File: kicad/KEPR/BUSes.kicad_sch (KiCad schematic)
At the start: 0 parts

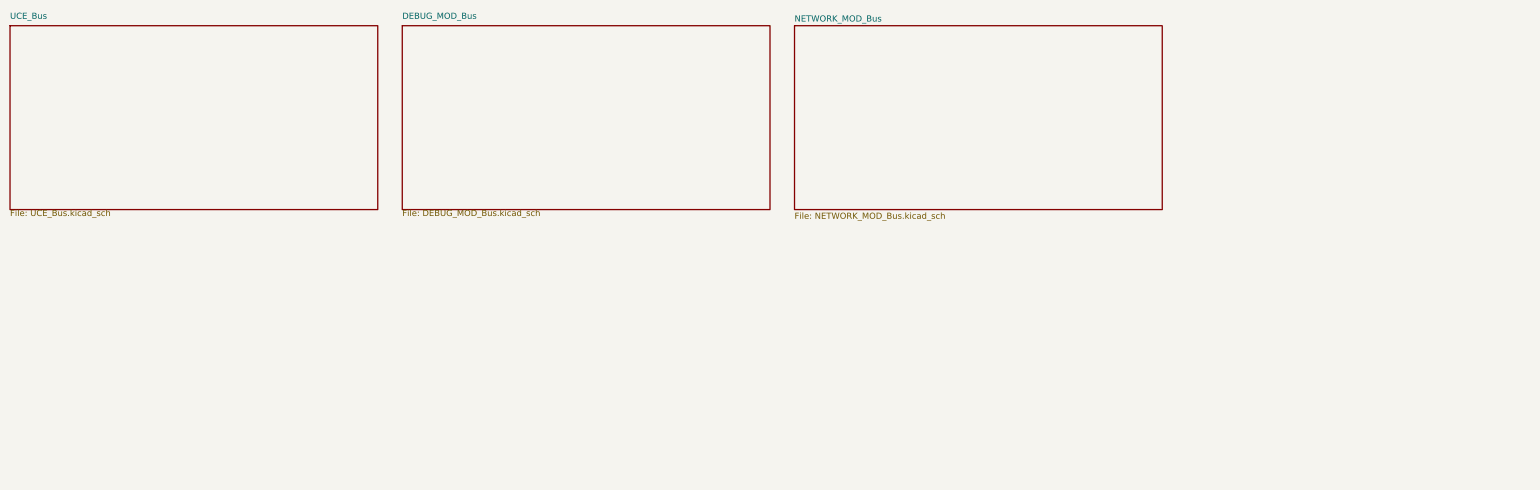
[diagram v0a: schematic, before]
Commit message: Definido os demais buses, criado folha do carimbo, versão 0.5
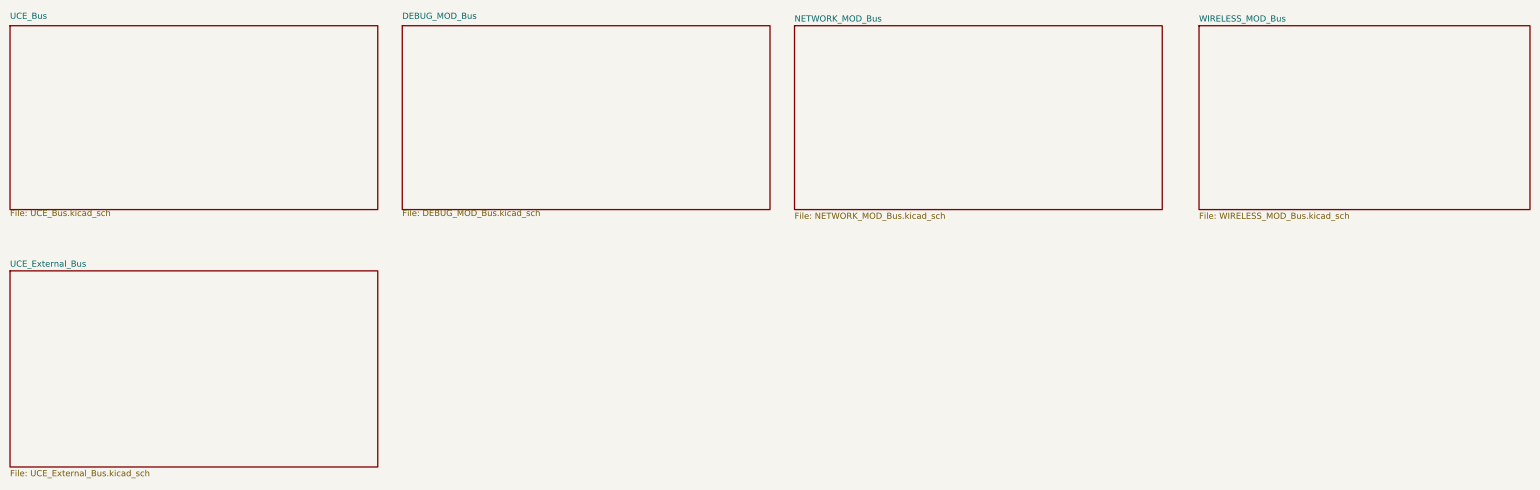
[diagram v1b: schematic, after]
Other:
- added sheet UCE_External_Bus (UCE_External_Bus.kicad_sch)
- added sheet WIRELESS_MOD_Bus (WIRELESS_MOD_Bus.kicad_sch)
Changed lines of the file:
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@@
 		)
 		(fill
-			(color 0 0 0 0.0000)
+			(color 255 73 85 1.0000)
 		)
 		(property "Sheetname" "DEBUG_MOD_Bus"
@@
 			(project "KEPR"
 				(path "/5d9e1dfb-5ec5-4e06-bbdb-9cbfa1c0b9f1/0260e008-78ae-4c2c-85f8-b31739d2ea08"
-					(page "1")
+					(page "A00103")
+				)
+			)
+		)
+	)
+	(sheet
+		(at 33.02 76.2)
+		(size 76.2 40.64)
+		(exclude_from_sim no)
+		(in_bom yes)
+		(on_board yes)
+		(dnp no)
+		(fields_autoplaced yes)
+		(stroke
+			(width 0.1524)
+			(type solid)
+		)
+		(fill
+			(color 255 75 79 1.0000)
+		)
+		(property "Sheetname" "UCE_External_Bus"
+			(at 33.02 75.4884 0)
+			(effects
+				(font
+					(size 1.27 1.27)
+				)
+				(justify left bottom)
+			)
+		)
+		(property "Sheetfile" "UCE_External_Bus.kicad_sch"
+			(at 33.02 117.4246 0)
+			(effects
+				(font
+					(size 1.27 1.27)
+				)
+				(justify left top)
+			)
+		)
+		(instances
+			(project "KEPR"
+				(path "/5d9e1dfb-5ec5-4e06-bbdb-9cbfa1c0b9f1/0260e008-78ae-4c2c-85f8-b31739d2ea08"
+					(page "A00105")
 				)
 			)
@@
 		)
 		(fill
-			(color 0 0 0 0.0000)
+			(color 255 73 85 1.0000)
 		)
 		(property "Sheetname" "NETWORK_MOD_Bus"
@@
 			(project "KEPR"
 				(path "/5d9e1dfb-5ec5-4e06-bbdb-9cbfa1c0b9f1/0260e008-78ae-4c2c-85f8-b31739d2ea08"
-					(page "2")
+					(page "A00102")
+				)
+			)
+		)
+	)
+	(sheet
+		(at 279.4 25.4)
+		(size 68.58 38.1)
+		(exclude_from_sim no)
+		(in_bom yes)
+		(on_board yes)
+		(dnp no)
+		(fields_autoplaced yes)
+		(stroke
+			(width 0.1524)
+			(type solid)
+		)
+		(fill
+			(color 255 73 85 1.0000)
+		)
+		(property "Sheetname" "WIRELESS_MOD_Bus"
+			(at 279.4 24.6884 0)
+			(effects
+				(font
+					(size 1.27 1.27)
+				)
+				(justify left bottom)
+			)
+		)
+		(property "Sheetfile" "WIRELESS_MOD_Bus.kicad_sch"
+			(at 279.4 64.0846 0)
+			(effects
+				(font
+					(size 1.27 1.27)
+				)
+				(justify left top)
+			)
+		)
+		(instances
+			(project "KEPR"
+				(path "/5d9e1dfb-5ec5-4e06-bbdb-9cbfa1c0b9f1/0260e008-78ae-4c2c-85f8-b31739d2ea08"
+					(page "A00104")
 				)
 			)
@@
 		)
 		(fill
-			(color 0 0 0 0.0000)
+			(color 255 73 85 1.0000)
 		)
 		(property "Sheetname" "UCE_Bus"
@@
 			(project "KEPR"
 				(path "/5d9e1dfb-5ec5-4e06-bbdb-9cbfa1c0b9f1/0260e008-78ae-4c2c-85f8-b31739d2ea08"
-					(page "3")
+					(page "A00101")
 				)
 			)
